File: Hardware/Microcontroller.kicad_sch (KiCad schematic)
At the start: 26 parts, among them J1 GT-USB-7010ASV, SW2 KMR231NG, SW3 KMR231NG, U1 ESP32-S3-MINI-1

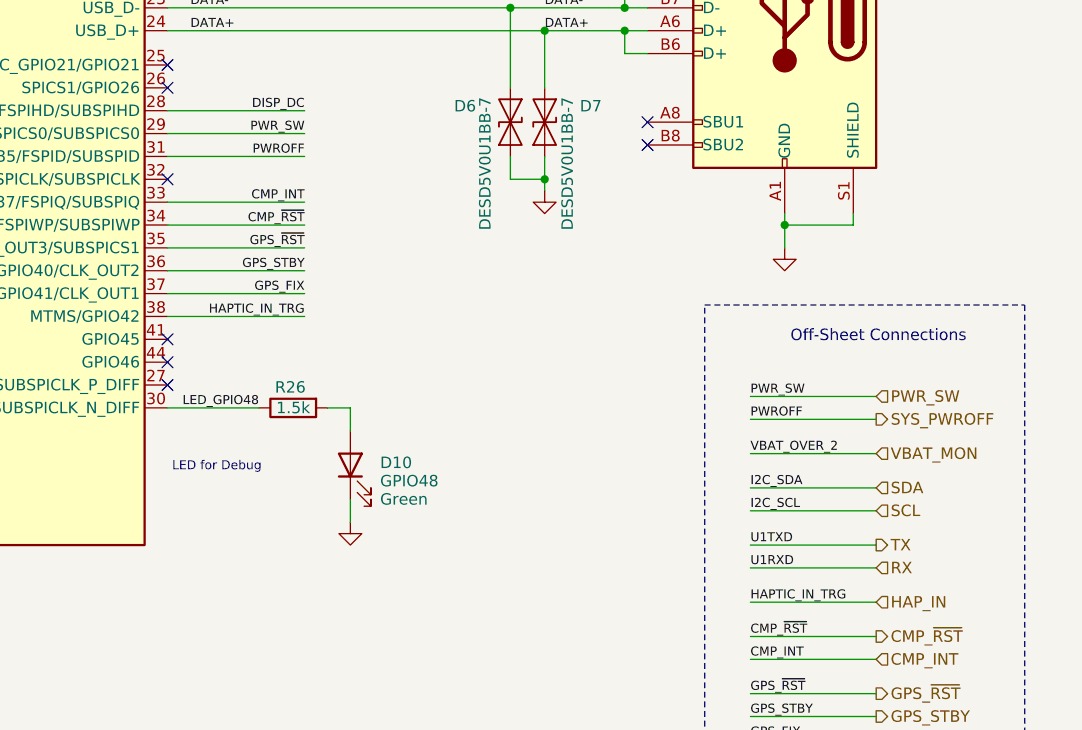
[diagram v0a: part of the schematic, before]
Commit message: sch: change USB Detect to SN74LVC1G14
Removed N-FET used, which had a problem of restarting the device
after powerdown when only powered by battery (no USB)
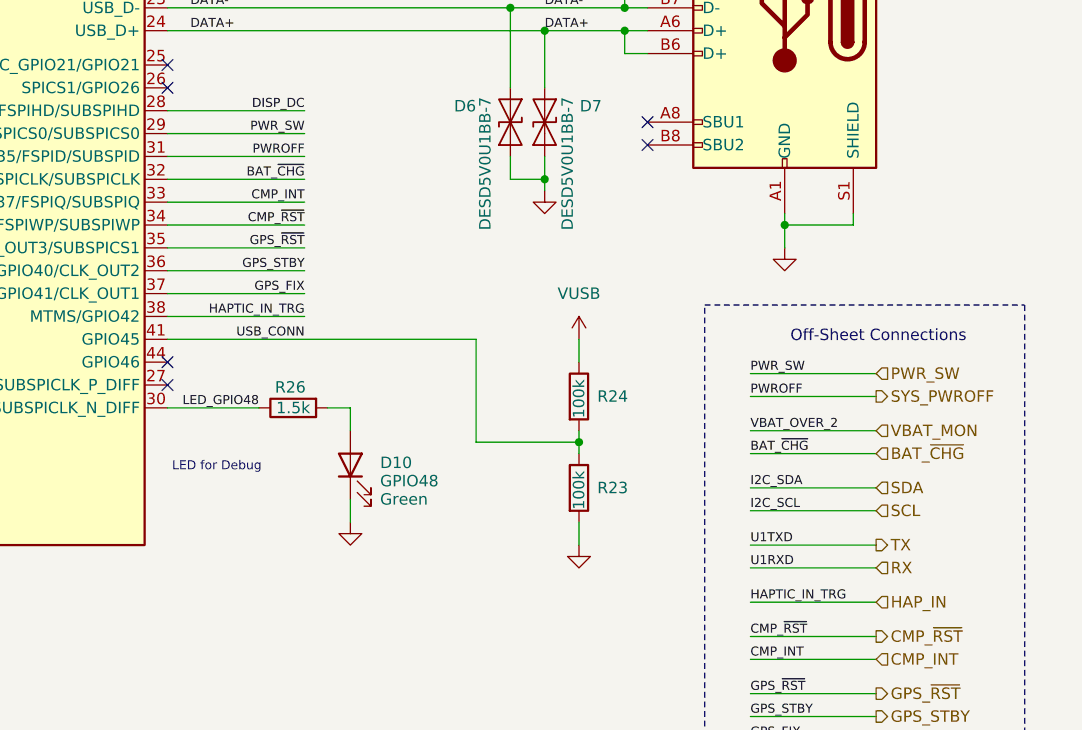
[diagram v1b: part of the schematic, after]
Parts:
- added R23, R24: 100k, Resistor_SMD:R_0603_1608Metric, symbol Device:R
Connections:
- net GND: now also R23.2
- net VUSB: now also R24.1
- net BAT_~{CHG}: now reaches U1.32 (SPIIO7/GPIO36/FSPICLK/SUBSPICLK)
- net USB_CONN: now reaches U1.41 (GPIO45)
- net USB_CONN: now also R23.1, R24.2
- no-connect marks 15 -> 13

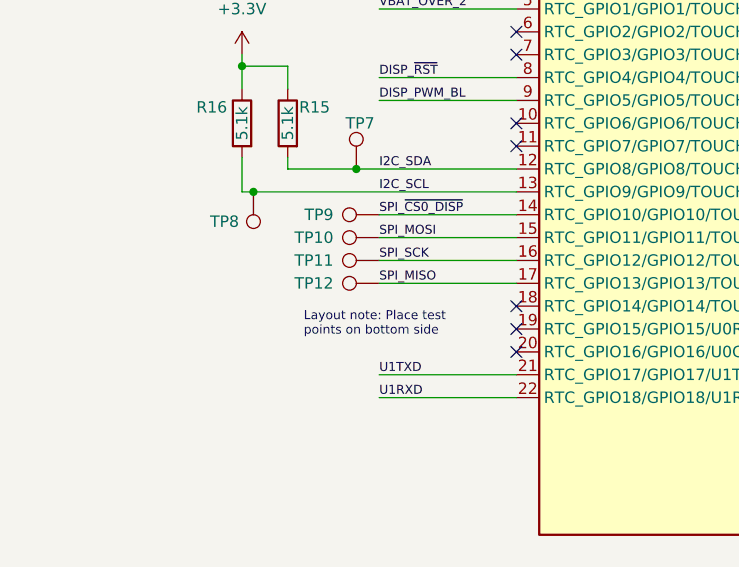
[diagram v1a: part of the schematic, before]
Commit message: pcb: move back graphics and tp. remove MISO tp.
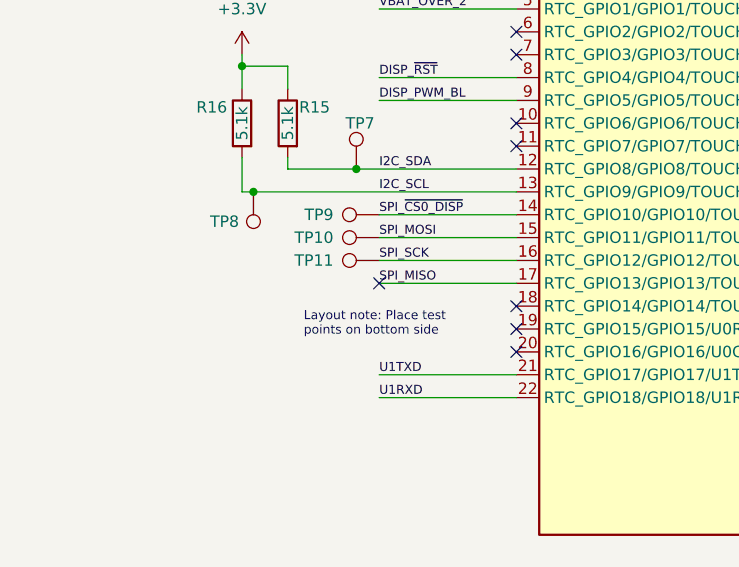
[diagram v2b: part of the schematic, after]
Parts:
- removed TP12: TXD0, M20048-1:TestPoint_Pad_D1.5mm_WITH_LABEL, symbol Connector:TestPoint
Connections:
- no-connect marks 13 -> 14
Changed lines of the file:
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@@
 	)
 	(no_connect
+		(at 53.34 96.52)
+	)
+	(no_connect
 		(at 187.96 71.12)
 	)
@@
 					(unit 1)
 				)
-			)
-		)
-	)
-	(symbol
-		(lib_id "Connector:TestPoint")
-		(at 53.34 96.52 90)
-		(mirror x)
-		(unit 1)
-		(exclude_from_sim no)
-		(in_bom no)
-		(on_board yes)
-		(dnp no)
-		(property "Reference" "TP12"
-			(at 48.26 96.52 90)
-			(effects
-				(font
-					(size 1.27 1.27)
-				)
-				(justify left)
-			)
-		)
-		(property "Value" "TXD0"
-			(at 48.26 97.7899 90)
-			(effects
-				(font
-					(size 1.27 1.27)
-				)
-				(justify left)
-				(hide yes)
-			)
-		)
-		(property "Footprint" "M20048-1:TestPoint_Pad_D1.5mm_WITH_LABEL"
-			(at 53.34 101.6 0)
-			(effects
-				(font
-					(size 1.27 1.27)
-				)
-				(hide yes)
-			)
-		)
-		(property "Datasheet" "~"
-			(at 53.34 101.6 0)
-			(effects
-				(font
-					(size 1.27 1.27)
-				)
-				(hide yes)
-			)
-		)
-		(property "Description" "test point"
-			(at 53.34 96.52 0)
-			(effects
-				(font
-					(size 1.27 1.27)
-				)
-				(hide yes)
-			)
-		)
-		(pin "1"
-		)
-		(instances
-			(project "Terra-HW"
-				(path "/acca4a2f-1cc7-44b0-a26a-921257f6c268/88b70e7a-287d-4532-b010-31738ffe5518"
-					(reference "TP12")
-					(unit 1)
-				)

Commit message: sch: updates
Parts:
- added TP12: RXD1, M20048-1:TestPoint_Pad_D1.5mm_WITH_LABEL, symbol Connector:TestPoint
- added TP14: TXD1, M20048-1:TestPoint_Pad_D1.5mm_WITH_LABEL, symbol Connector:TestPoint
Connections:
- net RX: now also TP12.1
- net TX: now also TP14.1
- net SYS_PWROFF renamed PWROFF
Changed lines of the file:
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@@
 	(title_block
 		(title "${TITLE}")
-		(date "2025-04-06")
+		(date "2025-08-29")
 		(rev "${REVISION}")
 		(company "${COMPANY}")
@@
 		)
 	)
-	(hierarchical_label "SYS_PWROFF"
-		(shape output)
-		(at 266.7 107.95 0)
-		(effects
-			(font
-				(size 1.27 1.27)
-			)
-			(justify left)
-		)
-	)
 	(hierarchical_label "GPS_STBY"
 		(shape output)
@@
 	)
 	(symbol
+		(lib_id "Connector:TestPoint")
+		(at 53.34 109.22 90)
+		(unit 1)
+		(exclude_from_sim no)
+		(in_bom no)
+		(on_board yes)
+		(dnp no)
+		(property "Reference" "TP12"
+			(at 48.26 109.22 90)
+			(effects
+				(font
+					(size 1.27 1.27)
+				)
+				(justify left)
+			)
+		)
+		(property "Value" "RXD1"
+			(at 48.26 107.9501 90)
+			(effects
+				(font
+					(size 1.27 1.27)
+				)
+				(justify left)
+				(hide yes)
+			)
+		)
+		(property "Footprint" "M20048-1:TestPoint_Pad_D1.5mm_WITH_LABEL"
+			(at 53.34 104.14 0)
+			(effects
+				(font
+					(size 1.27 1.27)
+				)
+				(hide yes)
+			)
+		)
+		(property "Datasheet" "~"
+			(at 53.34 104.14 0)
+			(effects
+				(font
+					(size 1.27 1.27)
+				)
+				(hide yes)
+			)
+		)
+		(property "Description" "test point"
+			(at 53.34 109.22 0)
+			(effects
+				(font
+					(size 1.27 1.27)
+				)
+				(hide yes)
+			)
+		)
+		(pin "1"
+		)
+		(instances
+			(project "Terra-HW"
+				(path "/acca4a2f-1cc7-44b0-a26a-921257f6c268/88b70e7a-287d-4532-b010-31738ffe5518"
+					(reference "TP12")
+					(unit 1)
+				)
+			)
+		)
+	)
+	(symbol
 		(lib_id "Device:C")
 		(at 137.16 39.37 0)
@@
 					(unit 1)
 				)
+			)
+		)
+	)
+	(symbol
+		(lib_id "Connector:TestPoint")
+		(at 53.34 106.68 90)
+		(unit 1)
+		(exclude_from_sim no)
+		(in_bom no)
+		(on_board yes)
+		(dnp no)
+		(property "Reference" "TP14"
+			(at 48.26 106.68 90)
+			(effects
+				(font
+					(size 1.27 1.27)
+				)
+				(justify left)
+			)
+		)
+		(property "Value" "TXD1"
+			(at 48.26 105.4101 90)
+			(effects
+				(font
+					(size 1.27 1.27)
+				)
+				(justify left)
+				(hide yes)
+			)
+		)
+		(property "Footprint" "M20048-1:TestPoint_Pad_D1.5mm_WITH_LABEL"
+			(at 53.34 101.6 0)
+			(effects
+				(font
+					(size 1.27 1.27)
+				)
+				(hide yes)
+			)
+		)
+		(property "Datasheet" "~"
+			(at 53.34 101.6 0)
+			(effects
+				(font
+					(size 1.27 1.27)
+				)
+				(hide yes)
+			)
+		)
+		(property "Description" "test point"
+			(at 53.34 106.68 0)
+			(effects
+				(font
+					(size 1.27 1.27)
+				)
+				(hide yes)
+			)
+		)
+		(pin "1"
+		)
+		(instances
+			(project "Terra-HW"
+				(path "/acca4a2f-1cc7-44b0-a26a-921257f6c268/88b70e7a-287d-4532-b010-31738ffe5518"
+					(reference "TP14")
+					(unit 1)
+				)

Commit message: pcb: more layout; sch: remove gps_stby signal
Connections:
- net GPS_STBY: no longer names the net of U1.36 (MTDO/GPIO40/CLK_OUT2)
- no-connect marks 14 -> 15
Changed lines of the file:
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@@
+	)
+	(no_connect
+		(at 187.96 93.98)
 	)
 	(no_connect
@@
 	(wire
 		(pts
-			(xy 187.96 93.98) (xy 203.2 93.98)
-		)
-		(stroke
-			(width 0)
-			(type default)
-		)
-	)
-	(wire
-		(pts
 			(xy 106.68 128.27) (xy 109.22 128.27)
 		)
@@
 	(wire
 		(pts
+			(xy 220.98 54.61) (xy 224.79 54.61)
+		)
+		(stroke
+			(width 0)
+			(type default)
+		)
+	)
+	(wire
+		(pts
+			(xy 119.38 128.27) (xy 119.38 127)
+		)
+		(stroke
+			(width 0)
+			(type default)
+		)
+	)
+	(wire
+		(pts
+			(xy 35.56 147.32) (xy 35.56 148.59)
+		)
+		(stroke
+			(width 0)
+			(type default)
+		)
+	)
+	(wire
+		(pts
 			(xy 252.73 143.51) (xy 266.7 143.51)
-		)
-		(stroke
-			(width 0)
-			(type default)
-		)
-	)
-	(wire
-		(pts
-			(xy 220.98 54.61) (xy 224.79 54.61)
-		)
-		(stroke
-			(width 0)
-			(type default)
-		)
-	)
-	(wire
-		(pts
-			(xy 119.38 128.27) (xy 119.38 127)
-		)
-		(stroke
-			(width 0)
-			(type default)
-		)
-	)
-	(wire
-		(pts
-			(xy 35.56 147.32) (xy 35.56 148.59)
-		)
-		(stroke
-			(width 0)
-			(type default)
-		)
-	)
-	(wire
-		(pts
-			(xy 252.73 146.05) (xy 266.7 146.05)
 		)
 		(stroke
@@
 		)
 	)
-	(label "GPS_STBY"
-		(at 252.73 143.51 0)
-		(effects
-			(font
-				(size 1 1)
-			)
-			(justify left bottom)
-		)
-	)
 	(label "CC1"
 		(at 241.3 54.61 180)
@@
 		)
 	)
-	(label "GPS_STBY"
-		(at 203.2 93.98 180)
-		(effects
-			(font
-				(size 1 1)
-			)
-			(justify right bottom)
-		)
-	)
 	(label "SPI_MISO"
 		(at 53.34 96.52 0)
@@
 	)
 	(label "GPS_FIX"
-		(at 252.73 146.05 0)
+		(at 252.73 143.51 0)
 		(effects
 			(font
@@
 	(hierarchical_label "GPS_FIX"
 		(shape input)
-		(at 266.7 146.05 0)
+		(at 266.7 143.51 0)
 		(effects
 			(font
@@
 		(effects
 			(font
-				(size 1.27 1.27)
-			)
-			(justify left)
-		)
-	)
-	(hierarchical_label "GPS_STBY"
-		(shape output)
-		(at 266.7 143.51 0)
-		(effects
-			(font

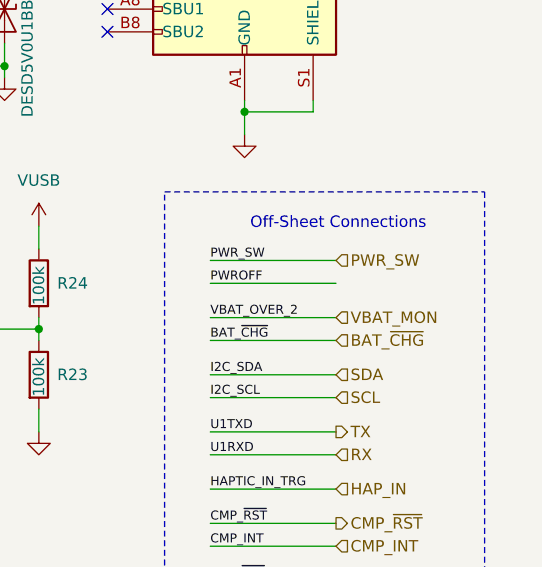
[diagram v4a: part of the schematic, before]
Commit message: pcb: final route + cleanup. sch: dnp gps conn.
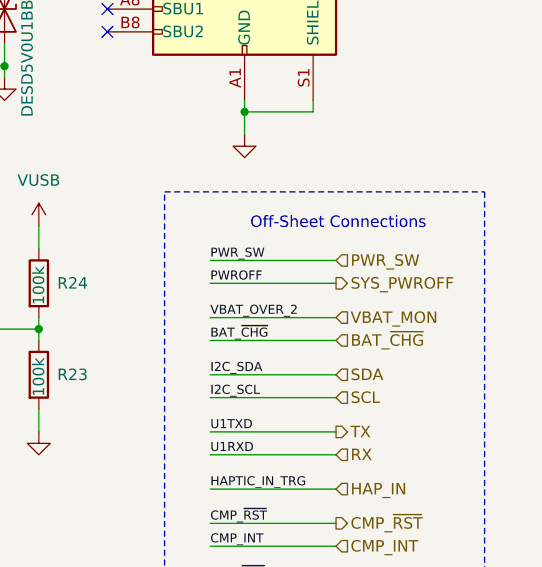
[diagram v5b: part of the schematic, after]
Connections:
- net PWROFF renamed SYS_PWROFF
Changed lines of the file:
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@@
+		)
+	)
+	(hierarchical_label "SYS_PWROFF"
+		(shape output)
+		(at 266.7 107.95 0)
+		(effects
+			(font
+				(size 1.27 1.27)
+			)
+			(justify left)
 		)
 	)

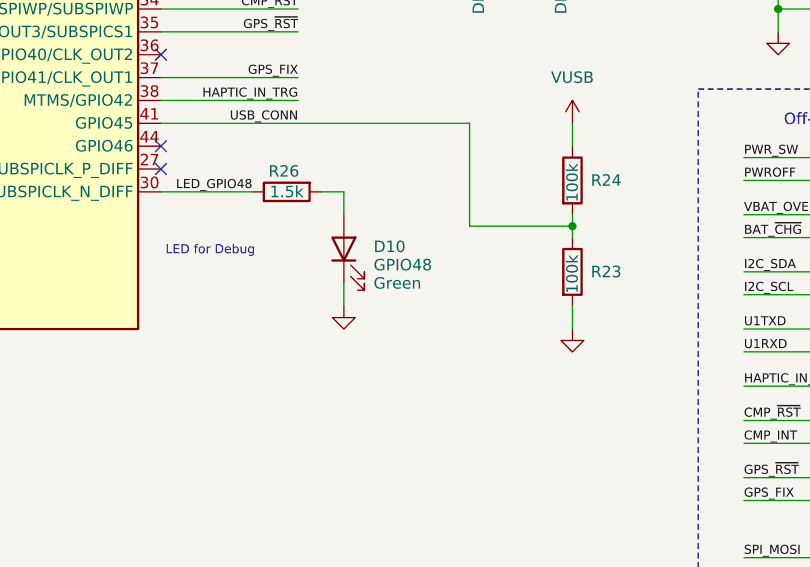
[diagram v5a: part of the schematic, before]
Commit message: change D10 to white and move near power button
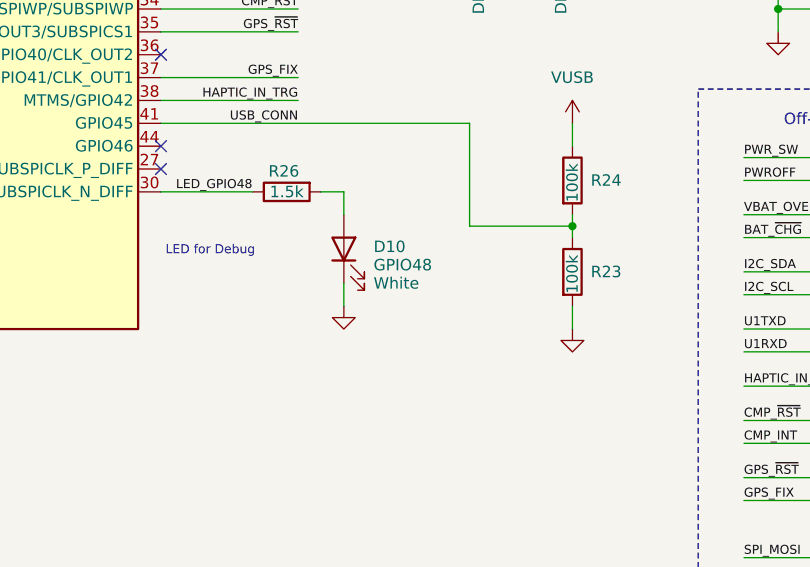
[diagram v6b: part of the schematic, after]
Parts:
- D10: MPN LTST-C190GKT -> IN-S63AT5UW
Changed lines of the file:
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@@
 			)
 		)
-		(property "Datasheet" "https://mm.digikey.com/Volume0/opasdata/d220001/medias/docus/858/LTST-C190GKT.pdf"
+		(property "Datasheet" "https://www.inolux-corp.com/datasheet/SMDLED/Mono%20Color%20Top%20View/IN-S63AT%20Series_V1.4.pdf"
 			(at 208.28 115.57 0)
 			(effects
@@
 			)
 		)
-		(property "Description" "Green"
+		(property "Description" "White"
 			(at 211.582 119.38 90)
 			(effects
@@
 			)
 		)
-		(property "MPN" "LTST-C190GKT"
+		(property "MPN" "IN-S63AT5UW"
 			(at 208.28 115.57 90)
 			(effects
